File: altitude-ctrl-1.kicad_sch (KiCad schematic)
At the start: 66 parts, among them J2 TC2030, J3 Conn_01x02, J4 Conn_01x02, J5 Conn_01x04_Pin, SW1 SW_Push, SW2 SW_Push, SW3 SW_Push, U1 SN65HVD230, U2 LM73100, U3 HT753-1, U4 STM32F103C8Tx, U5 LM73100, Y1 8M

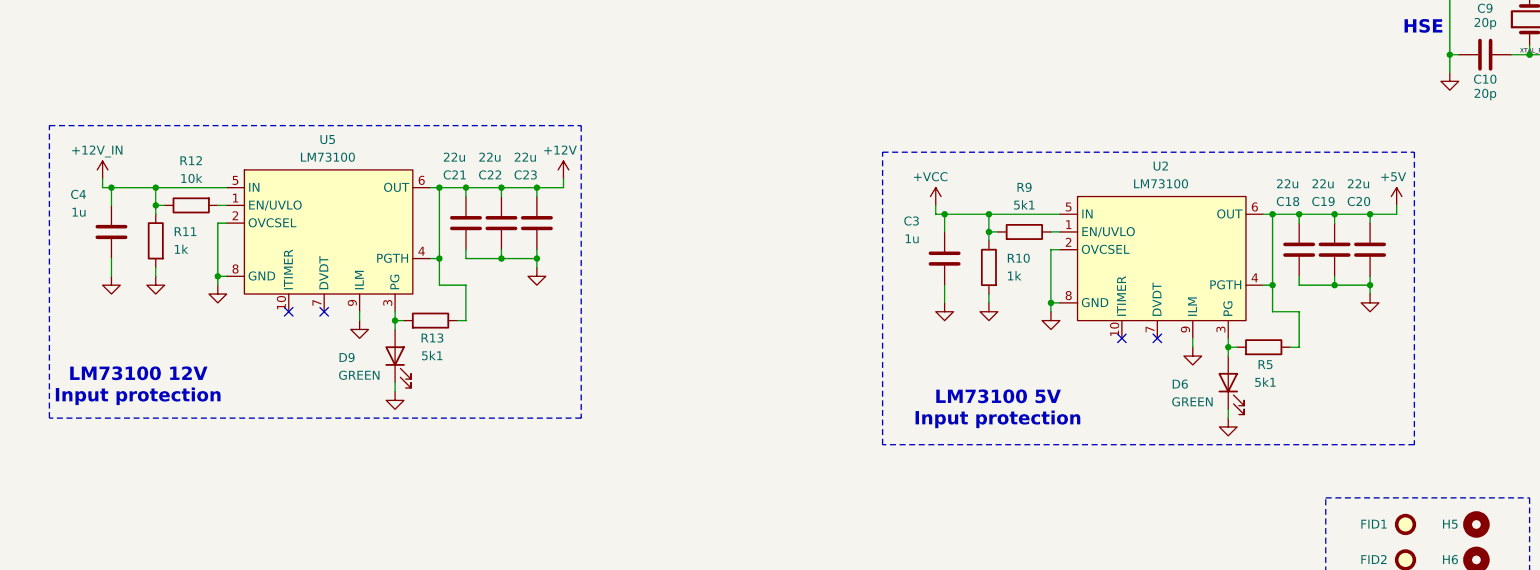
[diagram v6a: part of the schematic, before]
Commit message: schem: add input tvs
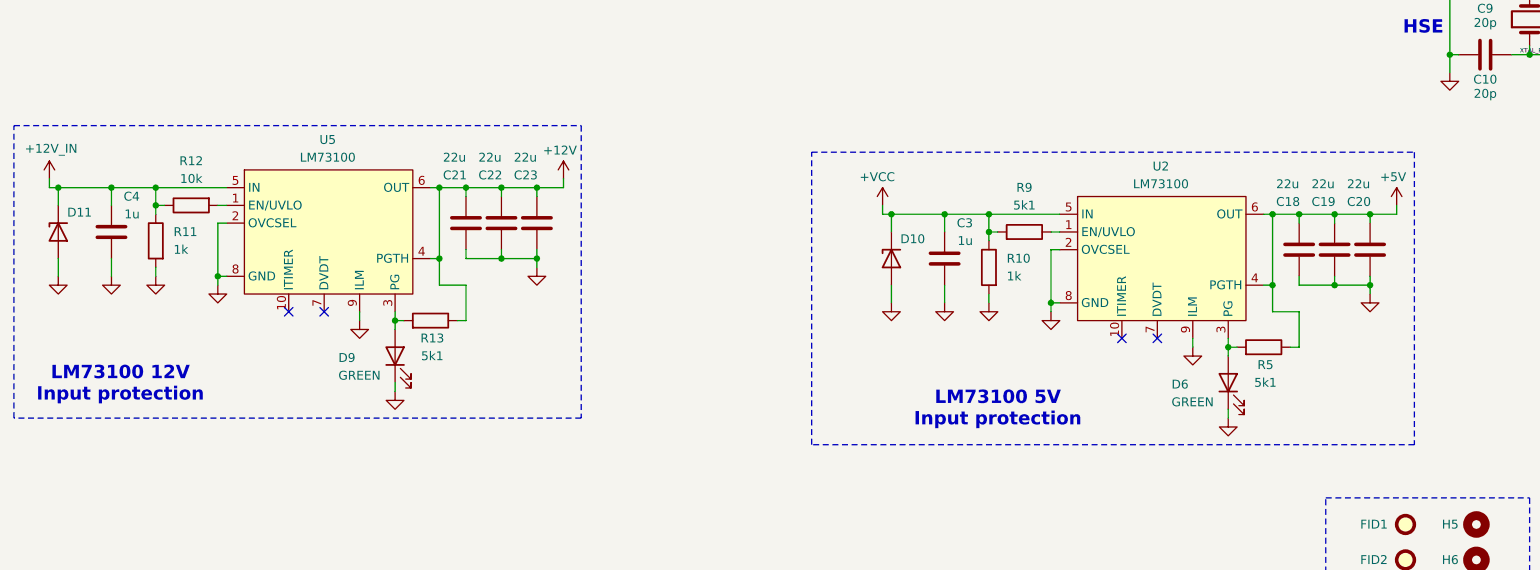
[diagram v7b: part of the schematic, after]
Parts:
- added D10, D11: SMAJ12A, Diode_SMD:D_SMA, symbol Pers:H5VU10U
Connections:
- net +12V_IN: now also D11.1 (K)
- net +VCC: now also D10.1 (K)
- net GND: now also D10.2 (A), D11.2 (A)

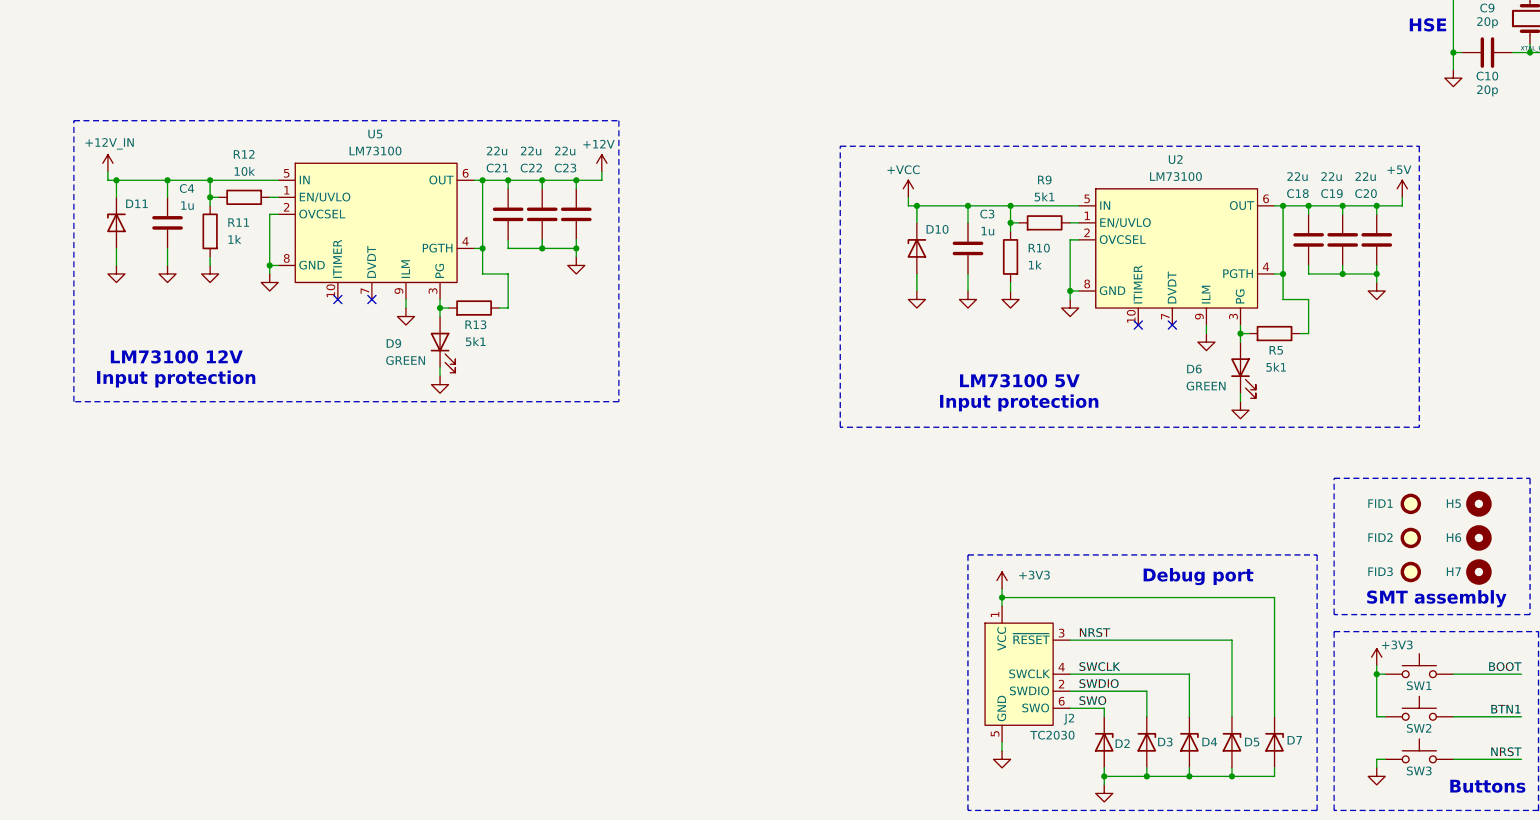
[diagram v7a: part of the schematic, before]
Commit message: schem: add power input conns
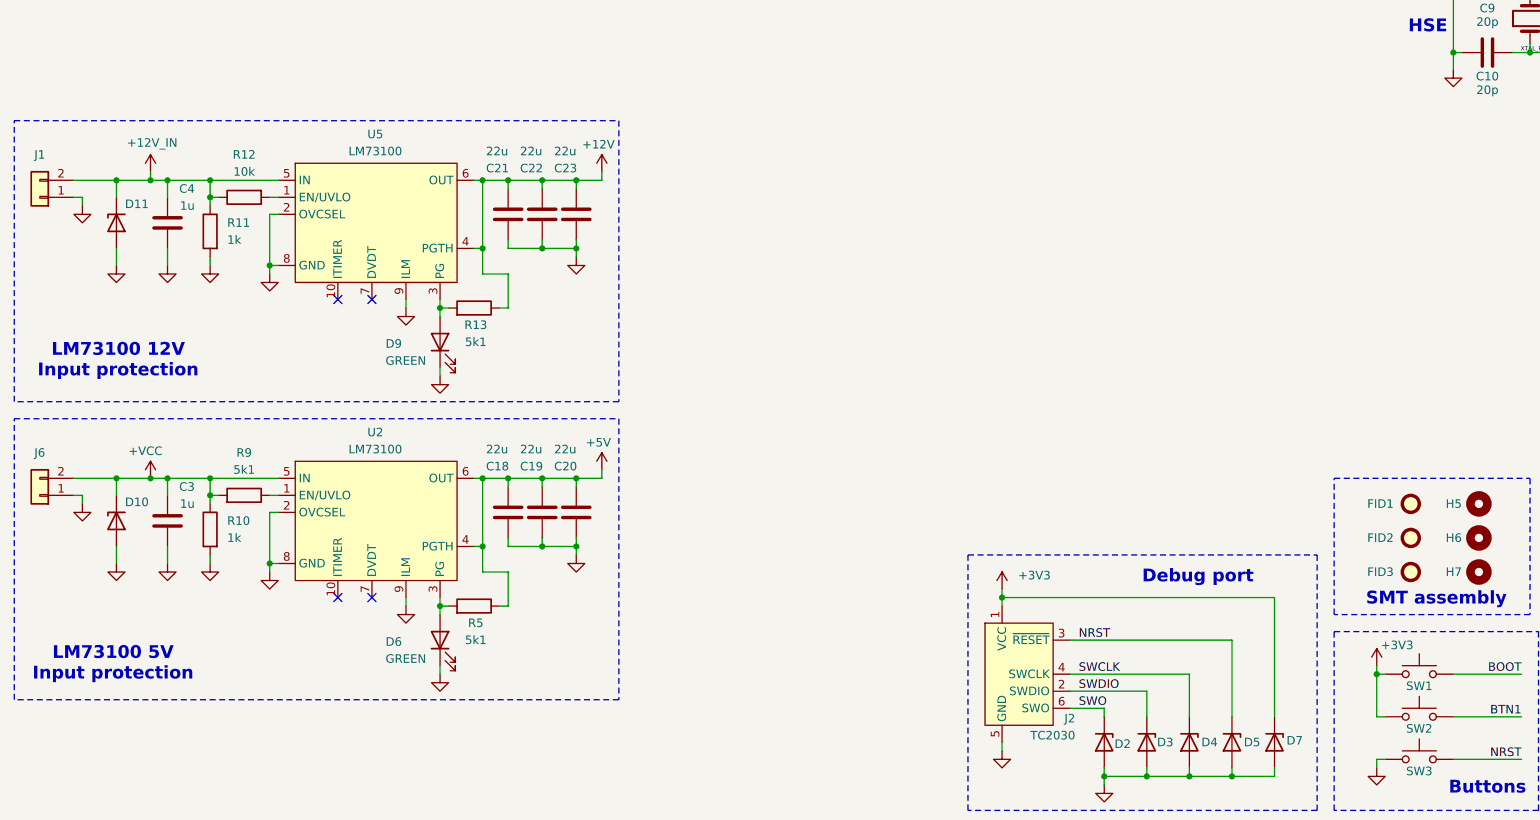
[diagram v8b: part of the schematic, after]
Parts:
- added J1, J6: Conn_01x02, symbol Connector_Generic:Conn_01x02
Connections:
- net +12V_IN: now also J1.2 (Pin_2)
- net +VCC: now also J6.2 (Pin_2)
- net GND: now also J1.1 (Pin_1), J6.1 (Pin_1)
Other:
- moved on the sheet: C18, C19, C20, C3, D10, D6, R10, R5, R9, U2
